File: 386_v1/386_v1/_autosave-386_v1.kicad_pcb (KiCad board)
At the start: 2 copper layers, 70 parts, among them U1 74LVC1G17GW, U2 74LVC1G17GW, U3 i386SX, U7 Conn_02x32_Odd_Even, U7A1 Conn_02x32_Odd_Even, U8 Conn_02x32_Odd_Even, U8A1 Conn_02x32_Odd_Even

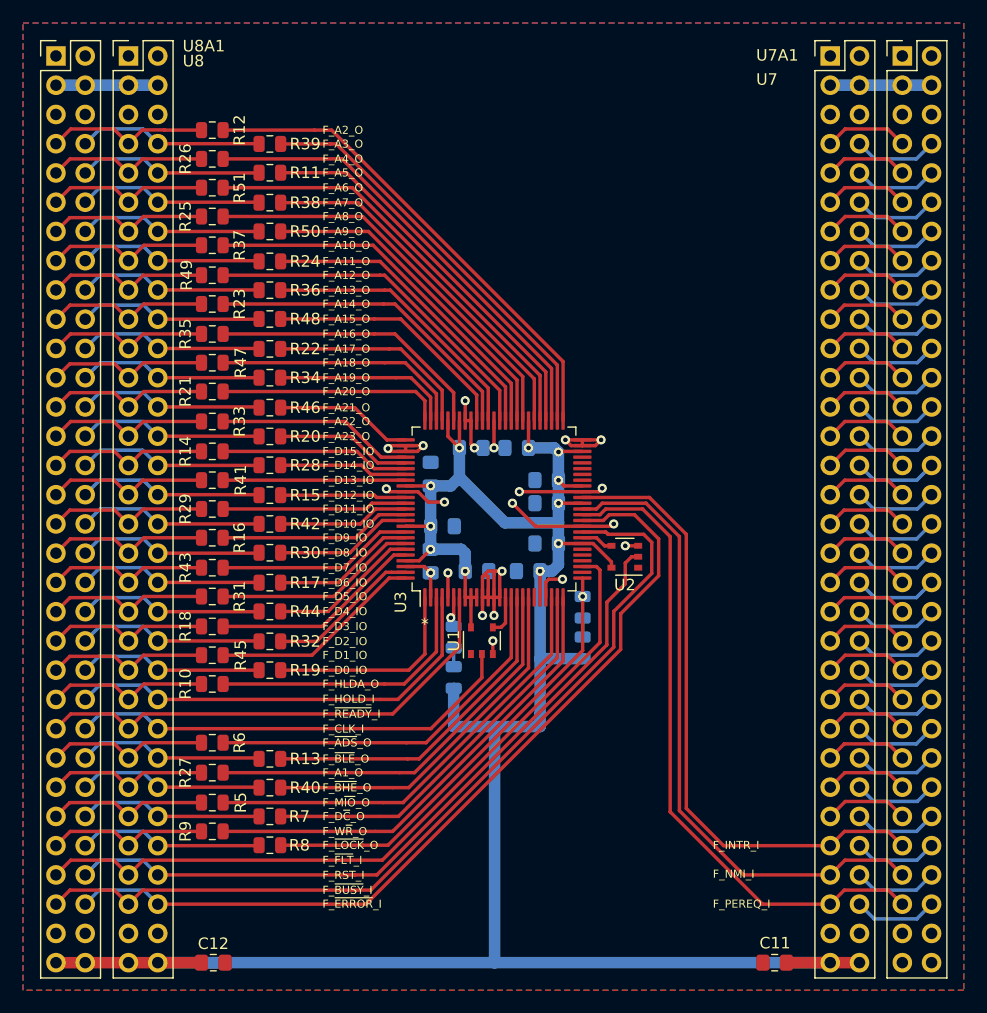
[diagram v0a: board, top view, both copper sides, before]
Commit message: use stack-trough connector
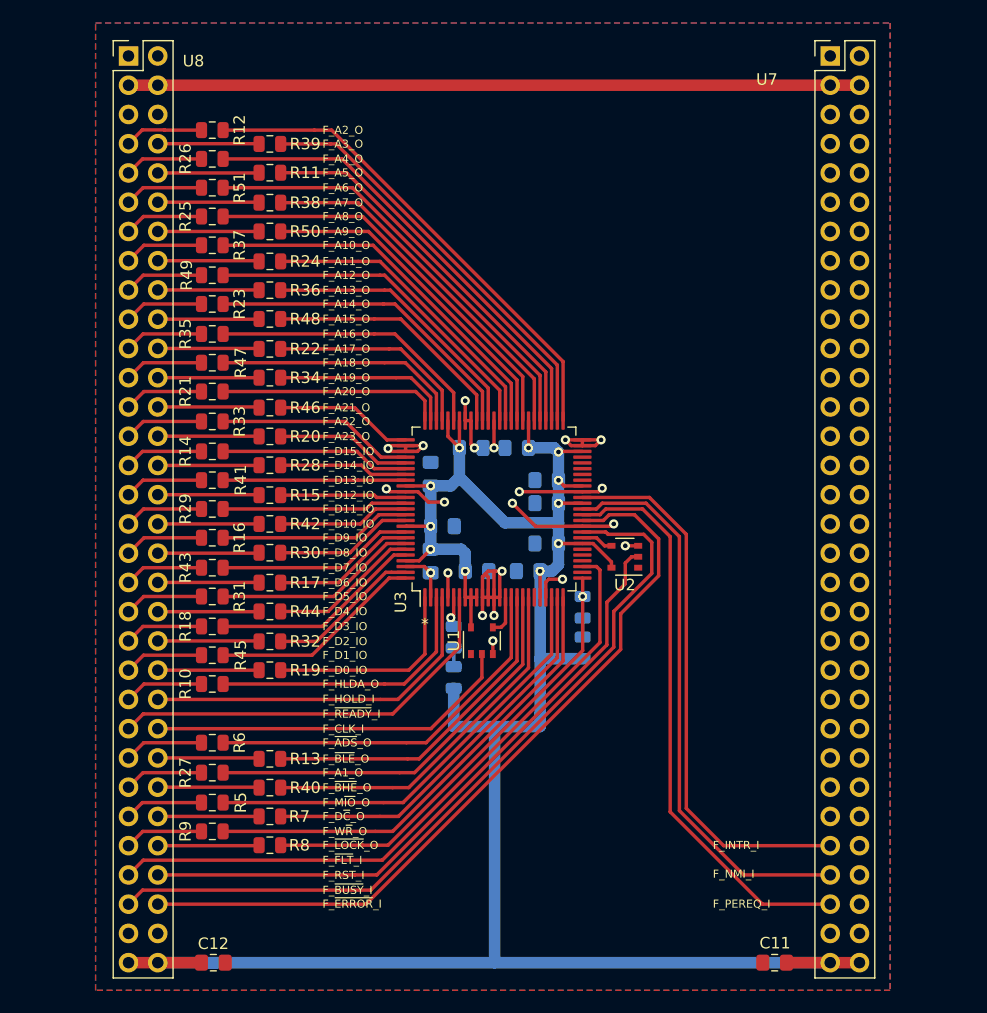
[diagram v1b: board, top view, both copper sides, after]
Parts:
- removed U7A1, U8A1: Conn_02x32_Odd_Even, Connector_PinHeader_2.54mm:PinHeader_2x32_P2.54mm_Vertical
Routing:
- net +3V3: track 17.6 -> 63.5 mm
- net /F_~BLE~_O: track 16.2 -> 8.83 mm
- net /F_D14_IO: track 16.2 -> 8.81 mm
- net /F_D10_IO: track 16.2 -> 8.80 mm
- net /F_A19_O: track 16.2 -> 8.80 mm
- net /12: track 7.37 -> 0.00 mm
- net /F_RST_I: track 63.7 -> 56.4 mm
- net /F_A2_O: track 14.2 -> 6.85 mm
- net /F_D7_IO: track 14.2 -> 6.87 mm
- net /F_A12_O: track 14.2 -> 6.87 mm
- net /F_A3_O: track 16.2 -> 8.81 mm
- net /F_D6_IO: track 16.2 -> 8.81 mm
- net /F_A13_O: track 16.2 -> 8.81 mm
- net /F_~READY~_I: track 43.4 -> 36.0 mm
- net /F_~FLT~_I: track 64.6 -> 57.2 mm
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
